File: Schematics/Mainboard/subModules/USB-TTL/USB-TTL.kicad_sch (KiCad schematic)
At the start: 7 parts, among them J1 Input, J2 Output, Q1 DTC143T, Q2 DTC143T, U1 CH340B

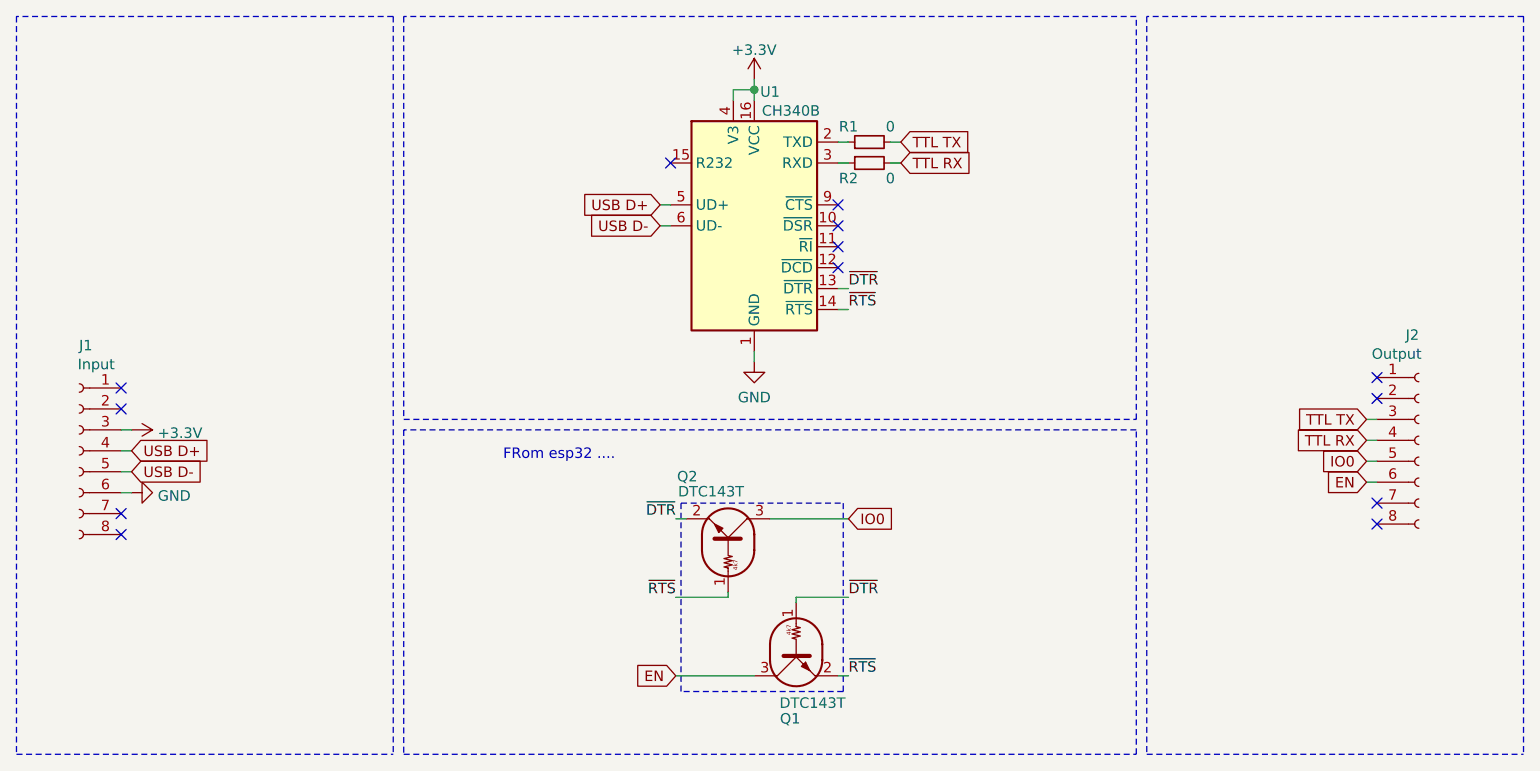
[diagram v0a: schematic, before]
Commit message: USB-TTL 2cm
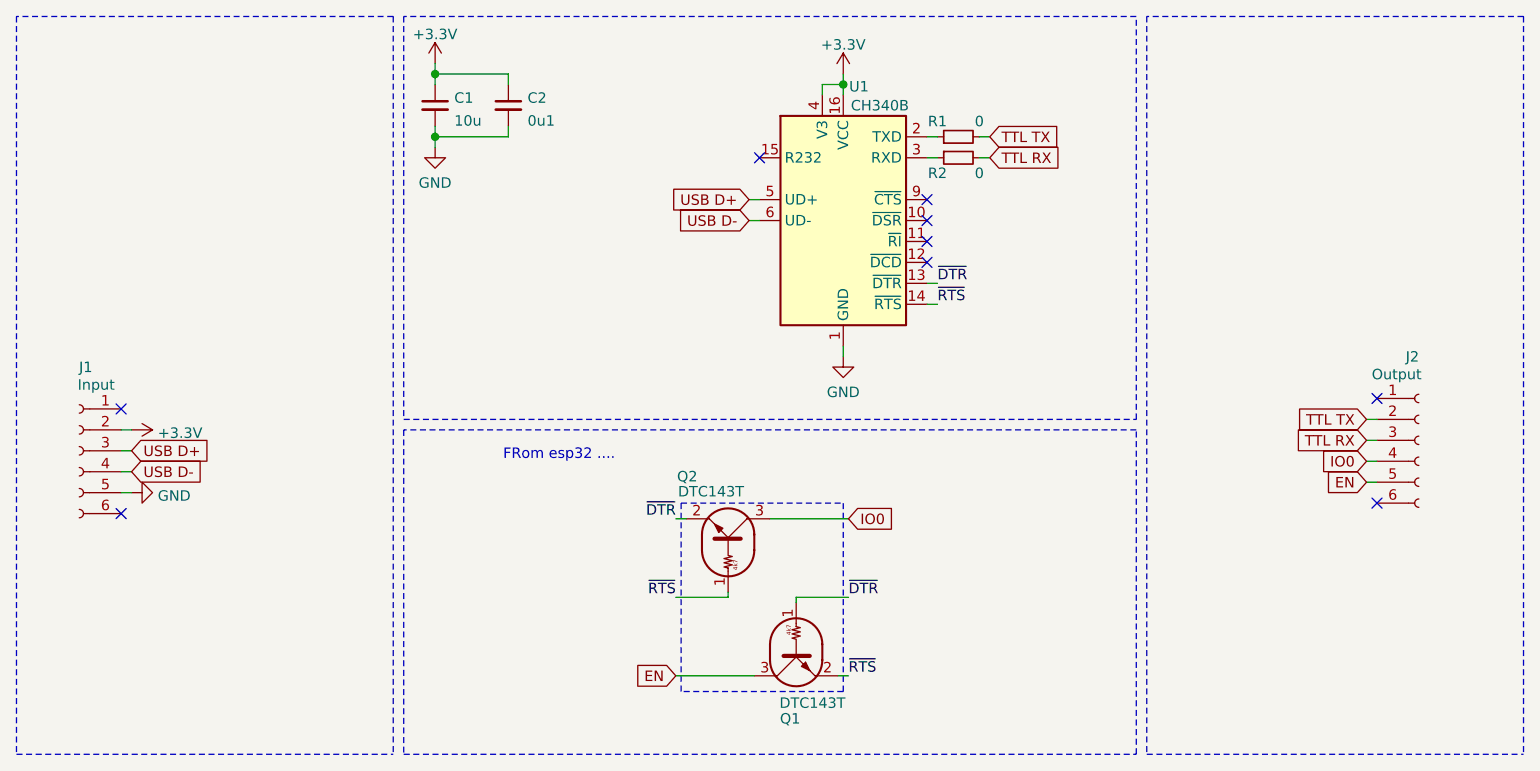
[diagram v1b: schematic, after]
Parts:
- removed J1: Input, Connector_PinSocket_2.54mm:PinSocket_1x08_P2.54mm_Vertical, symbol Connector:Conn_01x08_Female
- removed J2: Output, Connector_PinSocket_2.54mm:PinSocket_1x08_P2.54mm_Vertical, symbol Connector:Conn_01x08_Female
- added C1: 10u, Capacitor_SMD:C_0603_1608Metric, symbol Device:C_Small
- added C2: 0u1, Capacitor_SMD:C_0603_1608Metric, symbol Device:C_Small
- added J1: Input, Connector_PinSocket_2.54mm:PinSocket_1x06_P2.54mm_Vertical, symbol Connector:Conn_01x06_Female
- added J2: Output, Connector_PinSocket_2.54mm:PinSocket_1x06_P2.54mm_Vertical, symbol Connector:Conn_01x06_Female
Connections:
- net +3V3: now also C1.1, C2.1, J1.2 (Pin_2)
- net EN: now also J2.5 (Pin_5)
- net GND: now also C1.2, C2.2, J1.5 (Pin_5)
- net IO0: now also J2.4 (Pin_4)
- net TTL RX: now also J2.3 (Pin_3)
- net TTL TX: now also J2.2 (Pin_2)
- net USB D+: now also J1.3 (Pin_3)
- net USB D-: now also J1.4 (Pin_4)
- no-connect marks 13 -> 9
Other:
- moved on the sheet: R1, R2, U1
